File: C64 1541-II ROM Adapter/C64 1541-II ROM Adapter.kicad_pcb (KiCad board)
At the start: 2 copper layers, 22.2 x 44.5 mm, 7 parts, among them J1 A14, J2 A15, J3 GND, U1 27C512

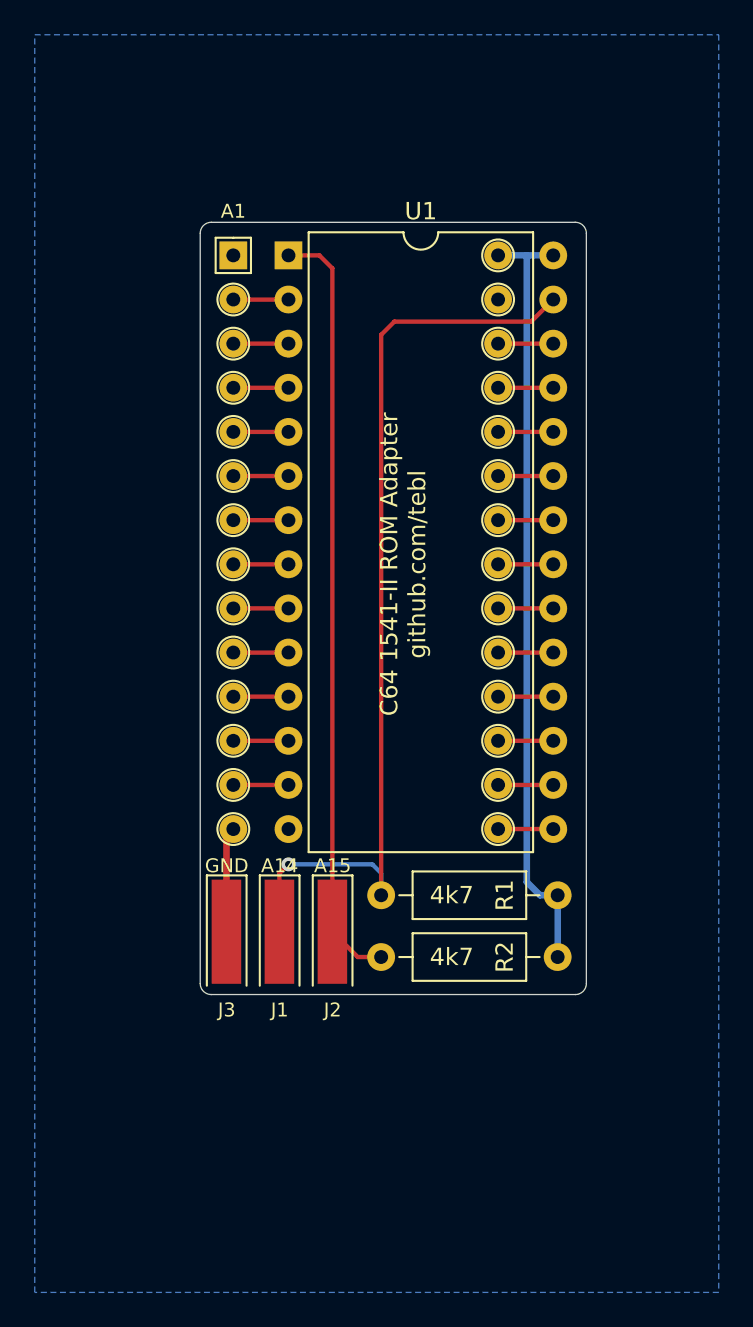
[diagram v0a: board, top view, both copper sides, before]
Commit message: Shorten ROM board a little bit
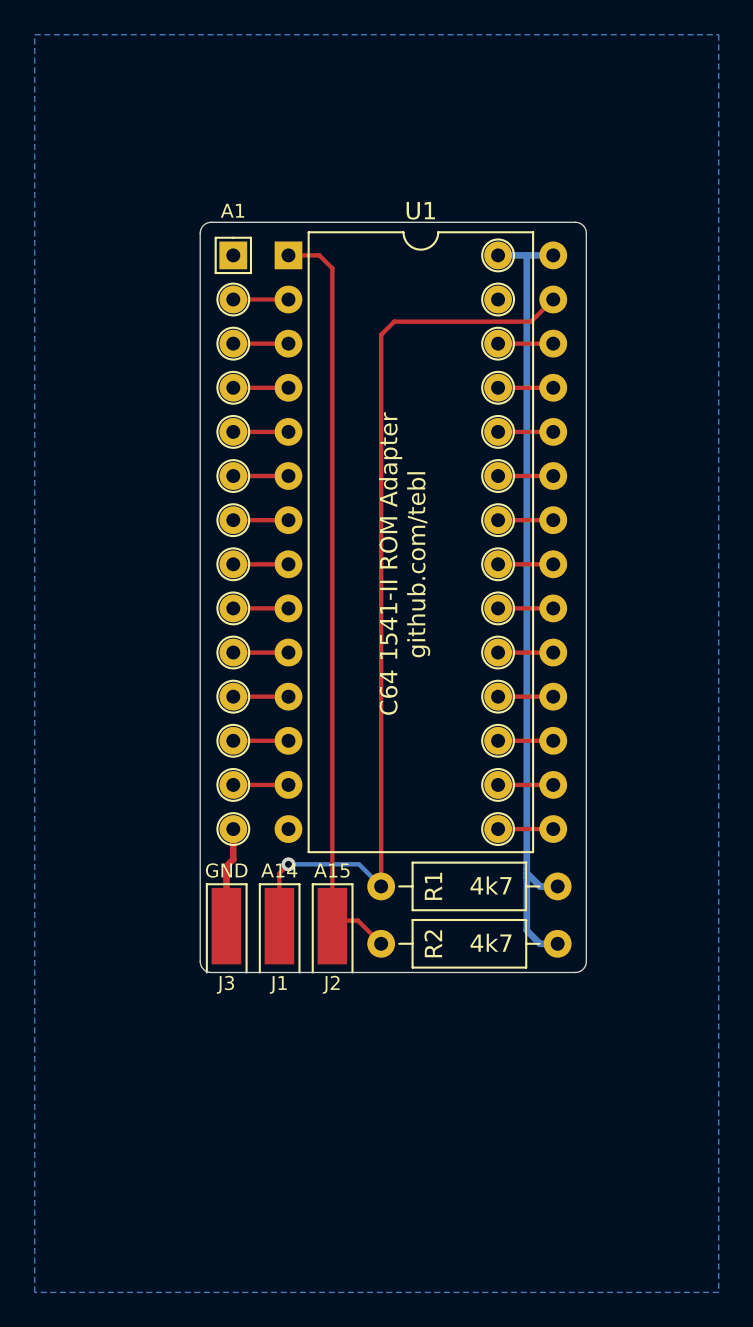
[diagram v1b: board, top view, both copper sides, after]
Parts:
- J1, J2, J3: footprint edge_connect:edge_pins_1x01 -> edge_connect:short_edge_pins_1x01
- moved R2 0.76 mm to (120.9, 101.9)
- moved J1 0.64 mm to (104.9, 100.5)
- moved J2 0.64 mm to (108.0, 100.5)
- moved J3 0.64 mm to (101.9, 100.5)
- moved R1 0.51 mm to (120.9, 98.6)
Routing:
- net VCC: track 44.9 -> 46.2 mm
- net /A14: track 53.9 -> 53.1 mm
- net /A15: track 44.4 -> 43.7 mm
- net GND: track 6.07 -> 5.43 mm
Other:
- board size 22.2 x 44.5 mm -> 22.2 x 43.2 mm
